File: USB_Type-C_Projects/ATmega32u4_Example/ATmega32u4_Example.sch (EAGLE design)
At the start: 54 parts, among them J1 105450-0101, J2 282834-3, J3 282834-3, J4 MF-CON-2.54mm-01x11, J5 MF-CON-2.54mm-01x11, SW1 MF-SW-TACT-4.2MM, U1 IP4234CZ6,125, U2 ATMEGA32U4-AU, X1 ABM3B-16.000MHZ-D-1-X-T

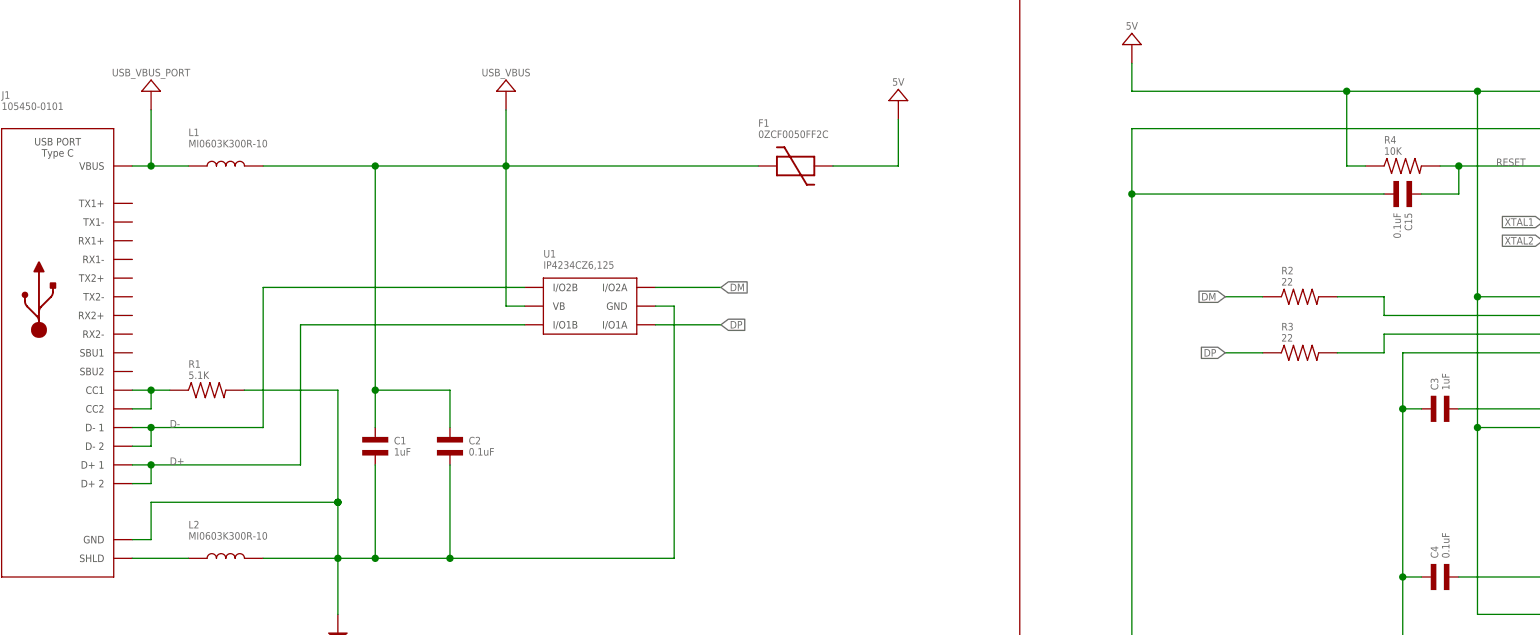
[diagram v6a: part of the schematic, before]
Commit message: updated with two (2 :O ) CC resistors
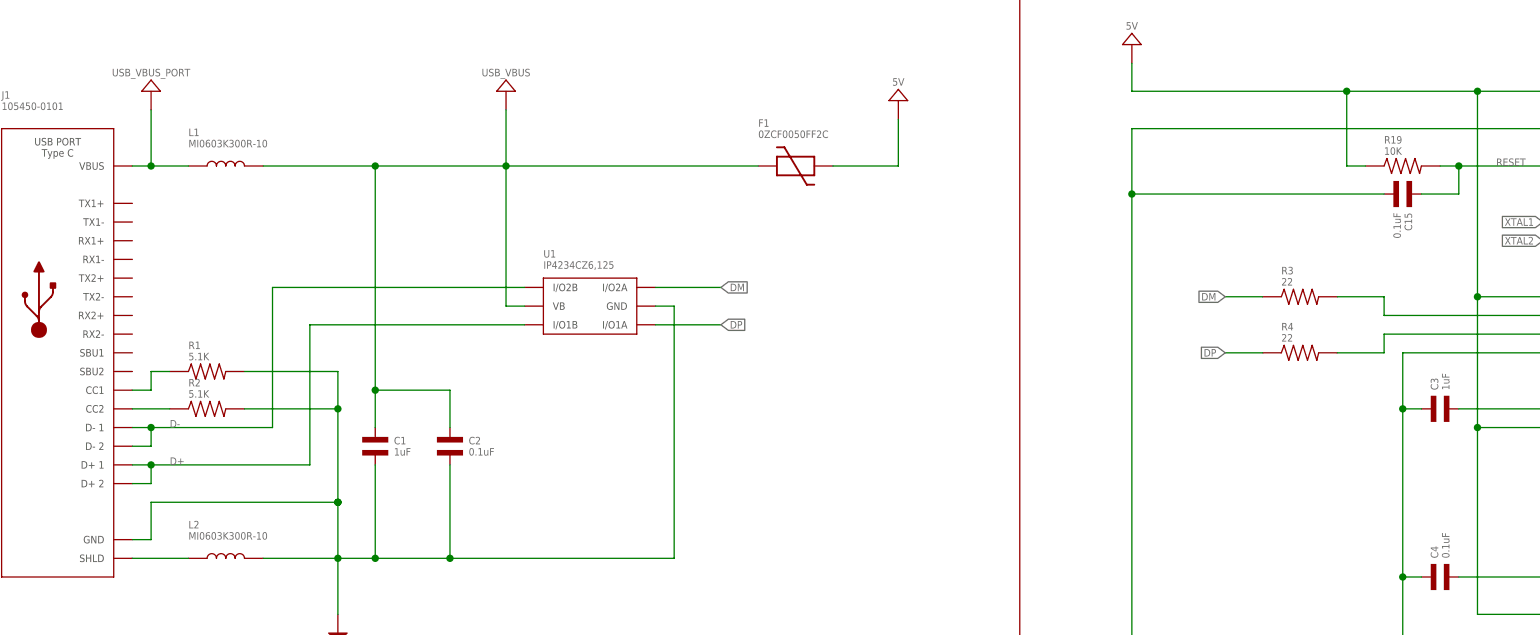
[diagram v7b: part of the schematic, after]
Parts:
- added R19: 10K, MF_Passives:RESISTOR_0603
- R2: value 22 -> 5.1K; MPN MF-RES-0603-22 -> ERJ-3EKF5101V
- R4: value 10K -> 22; MPN MF-RES-0603-10K -> MF-RES-0603-22
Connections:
- removed net CC1/1: J1.CC1, J1.CC2, R1.P$1
- new net CC1: J1.CC1, R1.P$1
- new net CC2: J1.CC2, R2.P$1
- net 5V: now also R19.P$1; no longer R4.P$1
- net DM: now also R3.P$1; no longer R2.P$1
- net DP: now also R4.P$1; no longer R3.P$1
- net GND: now also R2.P$2
- net N$1: now also R3.P$2; no longer R2.P$2
- net N$2: now also R4.P$2; no longer R3.P$2
- net RESET: now also R19.P$2; no longer R4.P$2
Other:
- moved on the sheet: R1, R2, R3, R4
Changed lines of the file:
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@@
 </part>
 <part name="U2" library="MF_IC_Digital" deviceset="ATMEGA32U4" device="-AU" value="ATMEGA32U4-AU"/>
-<part name="R2" library="MF_Passives" deviceset="RESISTOR" device="_0603" value="22">
+<part name="R3" library="MF_Passives" deviceset="RESISTOR" device="_0603" value="22">
 <attribute name="MPN" value="MF-RES-0603-22"/>
 </part>
-<part name="R3" library="MF_Passives" deviceset="RESISTOR" device="_0603" value="22">
+<part name="R4" library="MF_Passives" deviceset="RESISTOR" device="_0603" value="22">
 <attribute name="MPN" value="MF-RES-0603-22"/>
 </part>
@@
 <attribute name="MPN" value="MF-CAP-0603-0.1uF"/>
 </part>
-<part name="R4" library="MF_Passives" deviceset="RESISTOR" device="_0603" value="10K">
+<part name="R19" library="MF_Passives" deviceset="RESISTOR" device="_0603" value="10K">
 <attribute name="MPN" value="MF-RES-0603-10K"/>
 </part>
@@
 <attribute name="DNAME" value="Parker Dillmnan"/>
 <attribute name="REVNUM" value="REV: 2"/>
+</part>
+<part name="R2" library="MF_Passives" deviceset="RESISTOR" device="_0603" value="5.1K">
+<attribute name="MPN" value="ERJ-3EKF5101V"/>
 </part>
 </parts>
@@
 <attribute name="VALUE" x="67.31" y="190.5" size="1.016" layer="96" font="vector" align="center"/>
 </instance>
-<instance part="R1" gate="G$1" x="26.67" y="147.32" smashed="yes" rot="R90">
-<attribute name="NAME" x="24.13" y="151.384" size="1.016" layer="95" font="vector" align="top-left"/>
-<attribute name="VALUE" x="24.13" y="148.844" size="1.016" layer="96" font="vector"/>
+<instance part="R1" gate="G$1" x="26.67" y="149.86" smashed="yes" rot="R90">
+<attribute name="NAME" x="24.13" y="153.924" size="1.016" layer="95" font="vector" align="top-left"/>
+<attribute name="VALUE" x="24.13" y="151.384" size="1.016" layer="96" font="vector"/>
 </instance>
 <instance part="L1" gate="G$1" x="29.21" y="177.8" smashed="yes">
@@
 <attribute name="VALUE" x="212.09" y="193.04" size="1.016" layer="96" font="vector"/>
 </instance>
-<instance part="R2" gate="G$1" x="175.26" y="160.02" smashed="yes" rot="R90">
+<instance part="R3" gate="G$1" x="175.26" y="160.02" smashed="yes" rot="R90">
 <attribute name="NAME" x="172.72" y="164.084" size="1.016" layer="95" font="vector" align="top-left"/>
 <attribute name="VALUE" x="172.72" y="161.544" size="1.016" layer="96" font="vector"/>
 </instance>
-<instance part="R3" gate="G$1" x="175.26" y="152.4" smashed="yes" rot="R90">
+<instance part="R4" gate="G$1" x="175.26" y="152.4" smashed="yes" rot="R90">
 <attribute name="NAME" x="172.72" y="156.464" size="1.016" layer="95" font="vector" align="top-left"/>
 <attribute name="VALUE" x="172.72" y="153.924" size="1.016" layer="96" font="vector"/>
@@
 <attribute name="VALUE" x="195.58" y="124.46" size="1.016" layer="96" font="vector" rot="R90"/>
 </instance>
-<instance part="R4" gate="G$1" x="189.23" y="177.8" smashed="yes" rot="R90">
+<instance part="R19" gate="G$1" x="189.23" y="177.8" smashed="yes" rot="R90">
 <attribute name="NAME" x="186.69" y="181.864" size="1.016" layer="95" font="vector" align="top-left"/>
 <attribute name="VALUE" x="186.69" y="179.324" size="1.016" layer="96" font="vector"/>
@@
 <attribute name="DNAME" x="160.092" y="-3.762" size="2.54" layer="94" font="vector"/>
 </instance>
+<instance part="R2" gate="G$1" x="26.67" y="144.78" smashed="yes" rot="R90">
+<attribute name="NAME" x="24.13" y="148.844" size="1.016" layer="95" font="vector" align="top-left"/>
+<attribute name="VALUE" x="24.13" y="146.304" size="1.016" layer="96" font="vector"/>
+</instance>
 </instances>
 <busses>
@@
 <junction x="44.45" y="132.08"/>
 <wire x1="44.45" y1="132.08" x2="19.05" y2="132.08" width="0.1524" layer="91"/>
-<wire x1="31.75" y1="147.32" x2="44.45" y2="147.32" width="0.1524" layer="91"/>
-<wire x1="44.45" y1="147.32" x2="44.45" y2="132.08" width="0.1524" layer="91"/>
+<wire x1="31.75" y1="149.86" x2="44.45" y2="149.86" width="0.1524" layer="91"/>
+<wire x1="44.45" y1="149.86" x2="44.45" y2="144.78" width="0.1524" layer="91"/>
 <junction x="44.45" y="132.08"/>
+<wire x1="44.45" y1="144.78" x2="44.45" y2="132.08" width="0.1524" layer="91"/>
 <wire x1="34.29" y1="124.46" x2="44.45" y2="124.46" width="0.1524" layer="91"/>
 <wire x1="44.45" y1="124.46" x2="44.45" y2="132.08" width="0.1524" layer="91"/>
@@
 <pinref part="U1" gate="G$1" pin="GND"/>
 <wire x1="87.63" y1="158.75" x2="90.17" y2="158.75" width="0.1524" layer="91"/>
+<pinref part="R2" gate="G$1" pin="P$2"/>
+<wire x1="31.75" y1="144.78" x2="44.45" y2="144.78" width="0.1524" layer="91"/>
+<junction x="44.45" y="144.78"/>
 </segment>
 <segment>
@@
 <segment>
 <label x="21.59" y="137.16" size="1.016" layer="95" font="vector"/>
-<wire x1="39.37" y1="156.21" x2="39.37" y2="137.16" width="0.1524" layer="91"/>
-<wire x1="39.37" y1="137.16" x2="19.05" y2="137.16" width="0.1524" layer="91"/>
+<wire x1="40.64" y1="156.21" x2="40.64" y2="137.16" width="0.1524" layer="91"/>
+<wire x1="40.64" y1="137.16" x2="19.05" y2="137.16" width="0.1524" layer="91"/>
 <pinref part="J1" gate="G$1" pin="D+1"/>
 <wire x1="16.51" y1="137.16" x2="19.05" y2="137.16" width="0.1524" layer="91"/>
@@
 <wire x1="19.05" y1="134.62" x2="16.51" y2="134.62" width="0.1524" layer="91"/>
 <junction x="19.05" y="137.16"/>
-<wire x1="39.37" y1="156.21" x2="69.85" y2="156.21" width="0.1524" layer="91"/>
+<wire x1="40.64" y1="156.21" x2="69.85" y2="156.21" width="0.1524" layer="91"/>
 <pinref part="U1" gate="G$1" pin="I/O1B"/>
 </segment>
@@
 <segment>
 <label x="21.59" y="142.24" size="1.016" layer="95" font="vector"/>
-<wire x1="34.29" y1="161.29" x2="34.29" y2="142.24" width="0.1524" layer="91"/>
-<wire x1="34.29" y1="142.24" x2="19.05" y2="142.24" width="0.1524" layer="91"/>
+<wire x1="35.56" y1="161.29" x2="35.56" y2="142.24" width="0.1524" layer="91"/>
+<wire x1="35.56" y1="142.24" x2="19.05" y2="142.24" width="0.1524" layer="91"/>
 <pinref part="J1" gate="G$1" pin="D-1"/>
 <wire x1="16.51" y1="142.24" x2="19.05" y2="142.24" width="0.1524" layer="91"/>
@@
 <wire x1="19.05" y1="139.7" x2="16.51" y2="139.7" width="0.1524" layer="91"/>
 <junction x="19.05" y="142.24"/>
-<wire x1="34.29" y1="161.29" x2="69.85" y2="161.29" width="0.1524" layer="91"/>
+<wire x1="35.56" y1="161.29" x2="69.85" y2="161.29" width="0.1524" layer="91"/>
 <pinref part="U1" gate="G$1" pin="I/O2B"/>
 </segment>
@@
 </segment>
 </net>
-<net name="CC1/1" class="0">
+<net name="CC1" class="0">
 <segment>
 <pinref part="J1" gate="G$1" pin="CC1"/>
 <wire x1="16.51" y1="147.32" x2="19.05" y2="147.32" width="0.1524" layer="91"/>
-<wire x1="19.05" y1="147.32" x2="19.05" y2="144.78" width="0.1524" layer="91"/>
-<pinref part="J1" gate="G$1" pin="CC2"/>
-<wire x1="19.05" y1="144.78" x2="16.51" y2="144.78" width="0.1524" layer="91"/>
-<wire x1="19.05" y1="147.32" x2="21.59" y2="147.32" width="0.1524" layer="91"/>
-<junction x="19.05" y="147.32"/>
+<wire x1="19.05" y1="147.32" x2="19.05" y2="149.86" width="0.1524" layer="91"/>
+<wire x1="19.05" y1="149.86" x2="21.59" y2="149.86" width="0.1524" layer="91"/>
 <pinref part="R1" gate="G$1" pin="P$1"/>
 </segment>
@@
 </segment>
 <segment>
-<pinref part="R3" gate="G$1" pin="P$1"/>
+<pinref part="R4" gate="G$1" pin="P$1"/>
 <wire x1="170.18" y1="152.4" x2="165.1" y2="152.4" width="0.1524" layer="91"/>
 <label x="165.1" y="152.4" size="1.016" layer="95" font="vector" rot="R180" xref="yes"/>
@@
 </segment>
 <segment>
-<pinref part="R2" gate="G$1" pin="P$1"/>
+<pinref part="R3" gate="G$1" pin="P$1"/>
 <wire x1="170.18" y1="160.02" x2="165.1" y2="160.02" width="0.1524" layer="91"/>
 <label x="165.1" y="160.02" size="1.016" layer="95" font="vector" rot="R180" xref="yes"/>
@@
 <wire x1="209.55" y1="157.48" x2="186.69" y2="157.48" width="0.1524" layer="91"/>
 <wire x1="186.69" y1="157.48" x2="186.69" y2="160.02" width="0.1524" layer="91"/>
-<pinref part="R2" gate="G$1" pin="P$2"/>
+<pinref part="R3" gate="G$1" pin="P$2"/>
 <wire x1="186.69" y1="160.02" x2="180.34" y2="160.02" width="0.1524" layer="91"/>
 </segment>
@@
 <wire x1="209.55" y1="154.94" x2="186.69" y2="154.94" width="0.1524" layer="91"/>
 <wire x1="186.69" y1="154.94" x2="186.69" y2="152.4" width="0.1524" layer="91"/>
-<pinref part="R3" gate="G$1" pin="P$2"/>
+<pinref part="R4" gate="G$1" pin="P$2"/>
 <wire x1="186.69" y1="152.4" x2="180.34" y2="152.4" width="0.1524" layer="91"/>
 </segment>
@@
 <segment>
 <pinref part="U2" gate="G$1" pin="!RESET"/>
-<pinref part="R4" gate="G$1" pin="P$2"/>
+<pinref part="R19" gate="G$1" pin="P$2"/>
 <wire x1="209.55" y1="177.8" x2="196.85" y2="177.8" width="0.1524" layer="91"/>
 <label x="201.93" y="177.8" size="1.016" layer="95" font="vector"/>
@@
 <wire x1="199.39" y1="116.84" x2="199.39" y2="142.24" width="0.1524" layer="91"/>
 <junction x="199.39" y="142.24"/>
-<pinref part="R4" gate="G$1" pin="P$1"/>
+<pinref part="R19" gate="G$1" pin="P$1"/>
 <wire x1="184.15" y1="177.8" x2="181.61" y2="177.8" width="0.1524" layer="91"/>
 <wire x1="181.61" y1="177.8" x2="181.61" y2="187.96" width="0.1524" layer="91"/>
@@
 </segment>
 </net>
+<net name="CC2" class="0">
+<segment>
+<pinref part="J1" gate="G$1" pin="CC2"/>
+<pinref part="R2" gate="G$1" pin="P$1"/>
+<wire x1="16.51" y1="144.78" x2="21.59" y2="144.78" width="0.1524" layer="91"/>
+</segment>
+</net>
